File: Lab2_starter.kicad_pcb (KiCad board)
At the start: 4 copper layers, 123.2 x 64.6 mm, 79 parts, among them J1 973582101, J10 Conn_01x02, J11 Conn_01x02, J12 Conn_01x02, J13 Conn_01x02, J14 Conn_01x02, J15 Conn_01x02, J16 Conn_01x02, J2 973582100, J3 973582101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

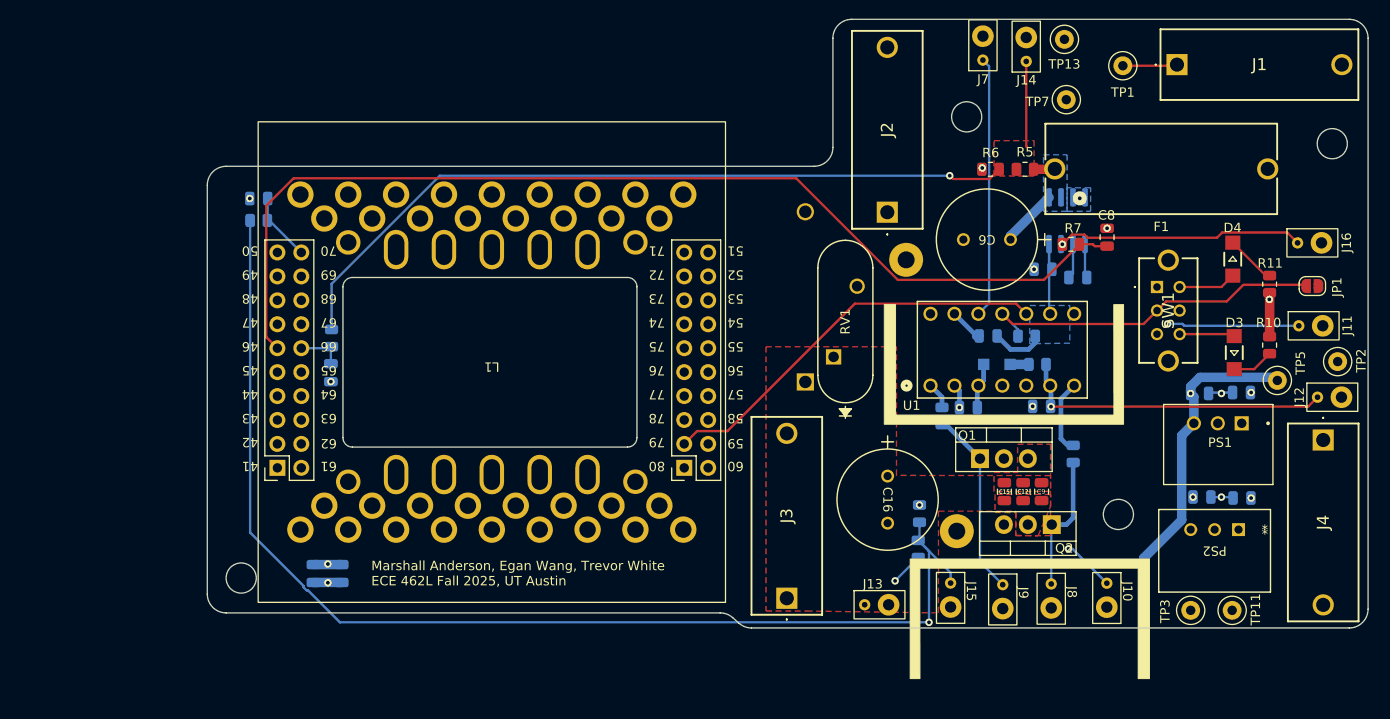
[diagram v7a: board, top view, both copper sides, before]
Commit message: Fixed DRC errors and reduced board size (again)
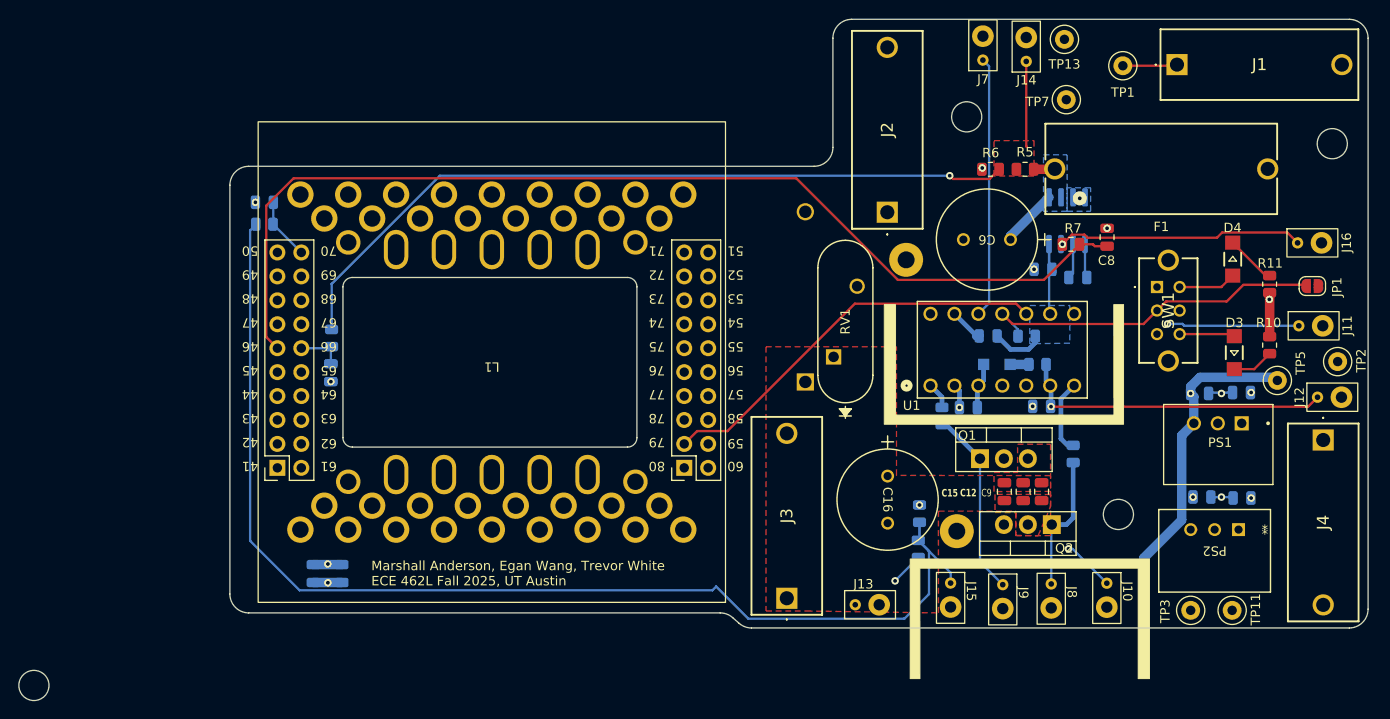
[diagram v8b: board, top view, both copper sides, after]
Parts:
- moved H1 24.8 mm to (12.6, 104.1)
- moved J13 1.00 mm to (101.0, 95.5)
- moved R8 0.72 mm to (37.1, 55.1)
- moved C11 0.72 mm to (37.1, 52.8)
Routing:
- net Vout: track 6.51 -> 0.16 mm
- net Vout_sens: track 126.3 -> 124.8 mm, vias 1 -> 0
- net /ADCINA0: track 7.36 -> 6.59 mm
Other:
- board size 123.2 x 64.6 mm -> 120.8 x 64.6 mm
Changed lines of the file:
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@@
 		(tags "capacitor")
 		(property "Reference" "C9"
-			(at 0 -0.05 180)
+			(at -0.13 -5.85 180)
 			(layer "F.SilkS")
 			(effects
 				(font
-					(size 0.5 0.5)
+					(size 0.8 0.6)
 					(thickness 0.1)
 				)
@@
 			(pinfunction "K")
 			(pintype "passive")
-			(solder_mask_margin 0.102)
+			(solder_mask_margin 0)
 		)
 		(pad "2" smd rect
@@
 			(pinfunction "A")
 			(pintype "passive")
-			(solder_mask_margin 0.102)
+			(solder_mask_margin 0)
 		)
 		(embedded_fonts no)
@@
 			(net 6 "+24V")
 			(pintype "passive")
-			(solder_mask_margin 0.102)
+			(solder_mask_margin 0)
 		)
 		(pad "2" thru_hole circle
@@
 			(net 75 "Vin")
 			(pintype "passive")
-			(solder_mask_margin 0.102)
+			(solder_mask_margin 0)
 		)
 		(embedded_fonts no)
@@
 	(footprint "ECE462L:TP"
 		(layer "F.Cu")
-		(at 102.041817 95.535)
+		(at 101.041817 95.535)
 		(property "Reference" "J13"
 			(at -0.41 -2.19 0)
@@
 		(tags "capacitor")
 		(property "Reference" "C8"
-			(at 2.327422 -0.06 180)
+			(at -2.472578 -0.06 180)
 			(layer "F.SilkS")
 			(effects
@@
 			(pinfunction "K")
 			(pintype "passive")
-			(solder_mask_margin 0.102)
+			(solder_mask_margin 0)
 		)
 		(pad "2" smd rect
@@
 			(pinfunction "A")
 			(pintype "passive")
-			(solder_mask_margin 0.102)
+			(solder_mask_margin 0)
 		)
 		(embedded_fonts no)
@@
 	(footprint "MountingHole:MountingHole_3.2mm_M3"
 		(layer "F.Cu")
-		(at 34.6 92.7)
+		(at 12.6 104.1)
 		(descr "Mounting Hole 3.2mm, no annular, M3")
 		(tags "mounting hole 3.2mm no annular m3")
@@
 			(pinfunction "VIN")
 			(pintype "input")
-			(solder_mask_margin 0.102)
+			(solder_mask_margin 0)
 		)
 		(pad "2" thru_hole circle
@@
 			(pinfunction "GND")
 			(pintype "power_in")
-			(solder_mask_margin 0.102)
+			(solder_mask_margin 0)
 		)
 		(pad "3" thru_hole circle
@@
 			(pinfunction "VOUT")
 			(pintype "output")
-			(solder_mask_margin 0.102)
+			(solder_mask_margin 0)
 		)
 		(embedded_fonts no)
@@
 		(tags "capacitor")
 		(property "Reference" "C12"
-			(at 0 -0.02 180)
+			(at -0.13 -5.82 180)
 			(layer "F.SilkS")
 			(effects
 				(font
-					(size 0.5 0.4)
+					(size 0.8 0.6)
 					(thickness 0.1)
 					(bold yes)
@@
 		(tags "capacitor")
 		(property "Reference" "C15"
-			(at -0.022578 0 180)
+			(at -0.152578 -5.8 180)
 			(layer "F.SilkS")
 			(effects
 				(font
-					(size 0.5 0.4)
+					(size 0.8 0.6)
 					(thickness 0.1)
 					(bold yes)
@@
 	(footprint "Resistor_SMD:R_0805_2012Metric"
 		(layer "B.Cu")
-		(at 36.459752 54.747916 180)
+		(at 37.059752 55.147916 180)
 		(descr "Resistor SMD 0805 (2012 Metric), square (rectangular) end terminal, IPC_7351 nominal, (Body size source: IPC-SM-782 page 72, https://www.pcb-3d.com/wordpress/wp-content/uploads/ipc-sm-782a_amendment_1_and_2.pdf), generated with kicad-footprint-generator")
 		(tags "resistor")
@@
 	(footprint "Capacitor_SMD:C_0805_2012Metric"
 		(layer "B.Cu")
-		(at 36.459752 52.420416 180)
+		(at 37.059752 52.820416 180)
 		(descr "Capacitor SMD 0805 (2012 Metric), square (rectangular) end terminal, IPC_7351 nominal, (Body size source: IPC-SM-782 page 76, https://www.pcb-3d.com/wordpress/wp-content/uploads/ipc-sm-782a_amendment_1_and_2.pdf, https://docs.google.com/spreadsheets/d/1BsfQQcO9C6DZCsRaXUlFlo91Tg2WpOkGARC1WS5S8t0/edit?usp=sharing), generated with kicad-footprint-generator")
 		(tags "capacitor")
 		(property "Reference" "C11"
-			(at 3.099752 -0.179584 180)
+			(at 0.099752 1.820416 180)
 			(layer "B.SilkS")
 			(effects
@@
 	)
 	(gr_arc
-		(start 33 96.4)
-		(mid 31.585786 95.814214)
-		(end 31 94.4)
+		(start 35.4 96.4)
+		(mid 33.985786 95.814214)
+		(end 33.4 94.4)
 		(stroke
 			(width 0.1)
@@
 	)
 	(gr_line
-		(start 33 96.4)
+		(start 35.4 96.4)
 		(end 85.439601 96.4)
 		(stroke
@@
 	)
 	(gr_arc
-		(start 31 51)
-		(mid 31.585786 49.585786)
-		(end 33 49)
+		(start 33.4 51)
+		(mid 33.985786 49.585786)
+		(end 35.4 49)
 		(stroke
 			(width 0.1)
@@
 	(gr_line
 		(start 95.4 49)
-		(end 33 49)
+		(end 35.4 49)
 		(stroke
 			(width 0.1)
@@
 	)
 	(gr_line
-		(start 31 94.4)
-		(end 31 51)
+		(start 33.4 94.4)
+		(end 33.4 51)
 		(stroke
 			(width 0.1)
@@
 	)
 	(via
-		(at 35.509752 52.420416)
+		(at 36.109752 52.820416)
 		(size 0.8)
 		(drill 0.4)
@@
 	)
 	(segment
-		(start 37.409752 52.420416)
-		(end 37.409752 54.710416)
+		(start 38.009752 55.110416)
+		(end 37.972252 55.147916)
 		(width 0.25)
 		(layer "B.Cu")
@@
 	)
 	(segment
-		(start 37.582916 54.747916)
-		(end 37.372252 54.747916)
+		(start 37.982916 55.147916)
+		(end 40.98 58.145)
 		(width 0.25)
 		(layer "B.Cu")
@@
 	)
 	(segment
-		(start 37.409752 54.710416)
-		(end 37.372252 54.747916)
+		(start 37.972252 55.147916)
+		(end 37.982916 55.147916)
 		(width 0.25)
 		(layer "B.Cu")
@@
 	)
 	(segment
-		(start 40.98 58.145)
-		(end 37.582916 54.747916)
+		(start 38.009752 52.820416)
+		(end 38.009752 55.110416)
 		(width 0.25)
 		(layer "B.Cu")
@@
 	)
 	(segment
-		(start 100.771817 95.535)
-		(end 94.415 95.535)
-		(width 0.25)
-		(layer "In1.Cu")
-		(net 11)
-	)
-	(segment
 		(start 139.535 66.812422)
 		(end 134.2 66.812422)
@@
 		(net 23)
 	)
-	(via
-		(at 107.6 97.4)
-		(size 0.8)
-		(drill 0.4)
-		(layers "F.Cu" "B.Cu")
-		(free yes)
-		(net 24)
-	)
 	(segment
-		(start 45.07525 97.4)
-		(end 107.6 97.4)
+		(start 84.601422 93.998578)
+		(end 40.798578 93.998578)
 		(width 0.25)
 		(layer "B.Cu")
@@
 	)
 	(segment
-		(start 35.547252 87.872002)
-		(end 41.211578 93.536328)
+		(start 40.798578 93.998578)
+		(end 35.547252 88.747252)
 		(width 0.25)
 		(layer "B.Cu")
@@
 	)
 	(segment
-		(start 41.542064 93.998578)
-		(end 41.673828 93.998578)
+		(start 109.891817 92.130737)
+		(end 109.891817 93.235)
 		(width 0.25)
 		(layer "B.Cu")
@@
 	)
 	(segment
-		(start 41.211578 93.536328)
-		(end 41.211578 93.668092)
+		(start 106.590248 86.773672)
+		(end 106.590248 88.568176)
 		(width 0.25)
 		(layer "B.Cu")
@@
 	)
 	(segment
-		(start 35.547252 54.747916)
-		(end 35.547252 87.872002)
+		(start 85 93.6)
+		(end 84.601422 93.998578)
 		(width 0.25)
 		(layer "B.Cu")
@@
 	)
 	(segment
-		(start 109.891817 92.130737)
-		(end 109.891817 93.235)
+		(start 106.459752 88.698672)
+		(end 107.6 89.83892)
 		(width 0.25)
 		(layer "B.Cu")
@@
 	)
 	(segment
-		(start 106.590248 86.773672)
-		(end 106.590248 88.568176)
+		(start 88.411 97.011)
+		(end 85 93.6)
 		(width 0.25)
 		(layer "B.Cu")
@@
 	)
 	(segment
-		(start 41.211578 93.668092)
-		(end 41.542064 93.998578)
+		(start 107.6 94.4)
+		(end 104.989 97.011)
 		(width 0.25)
 		(layer "B.Cu")
@@
 	)
 	(segment
-		(start 107.6 97.4)
-		(end 107.6 89.83892)
+		(start 107.6 89.83892)
+		(end 107.6 94.4)
 		(width 0.25)
 		(layer "B.Cu")
@@
 	)
 	(segment
-		(start 41.673828 93.998578)
-		(end 45.07525 97.4)
+		(start 35.547252 88.747252)
+		(end 35.547252 55.8)
 		(width 0.25)
 		(layer "B.Cu")
@@
 	)
 	(segment
-		(start 107.6 89.83892)
-		(end 106.459752 88.698672)
+		(start 36.147252 55.147916)
+		(end 36.147252 55.2)
+		(width 0.25)
+		(layer "B.Cu")
+		(net 24)
+	)
+	(segment
+		(start 36.147252 55.2)
+		(end 35.547252 55.8)
+		(width 0.25)
+		(layer "B.Cu")
+		(net 24)
+	)
+	(segment
+		(start 104.989 97.011)
+		(end 88.411 97.011)
 		(width 0.25)
 		(layer "B.Cu")
@@
 		(filled_areas_thickness no)
 		(keepout
-			(tracks not_allowed)
-			(vias not_allowed)
-			(pads not_allowed)
+			(tracks allowed)
+			(vias allowed)
+			(pads allowed)
 			(copperpour not_allowed)
 			(footprints allowed)
@@
 		(filled_areas_thickness no)
 		(keepout
-			(tracks not_allowed)
-			(vias not_allowed)
-			(pads not_allowed)
+			(tracks allowed)
+			(vias allowed)
+			(pads allowed)
 			(copperpour not_allowed)
 			(footprints allowed)
